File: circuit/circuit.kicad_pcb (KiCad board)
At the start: 2 copper layers, 51.5 x 59 mm, 19 parts, among them J5 PWR1, J6 Signal1, J7 PWR2, J8 Signal2, Q3 BC337, U5 ADuM1250, U6 Optocoupler_DC_PhotoNPN_AKEC, U7 LM7805

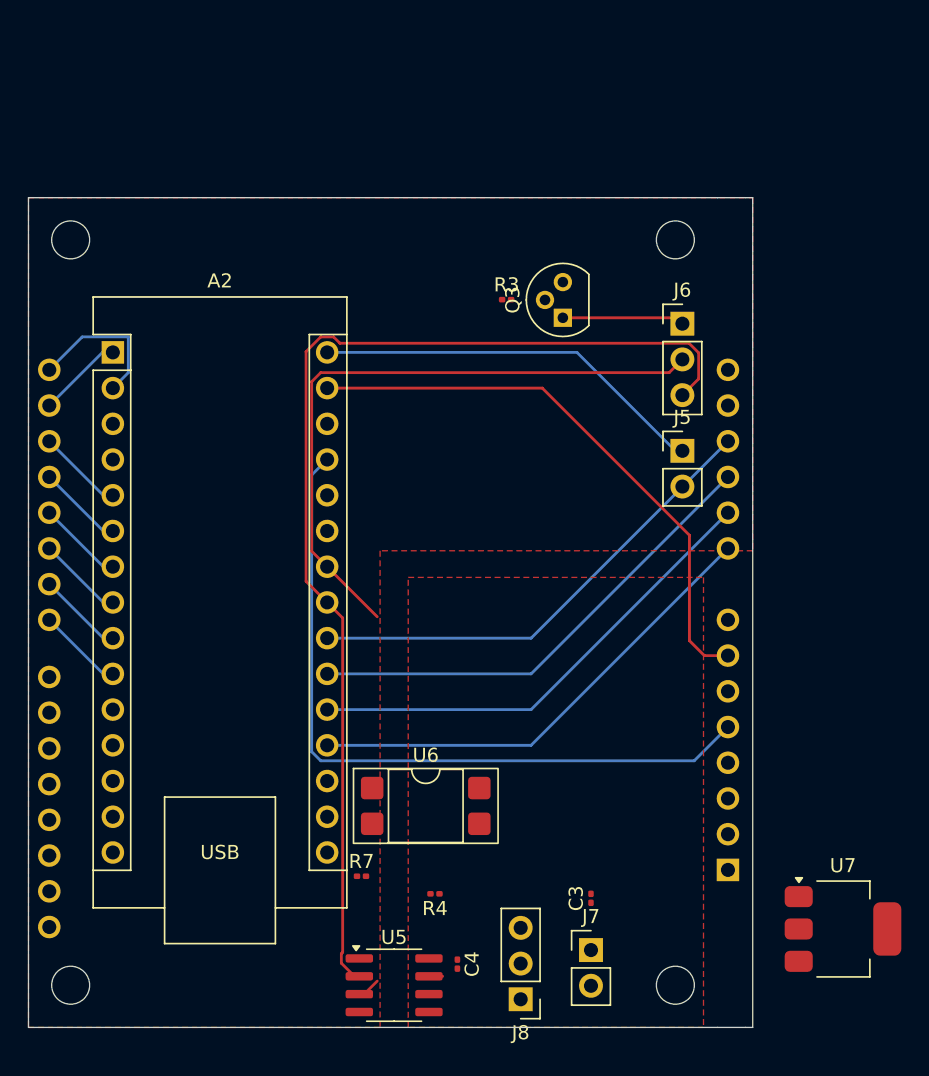
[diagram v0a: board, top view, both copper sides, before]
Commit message: Updated PCB layout and circuit.
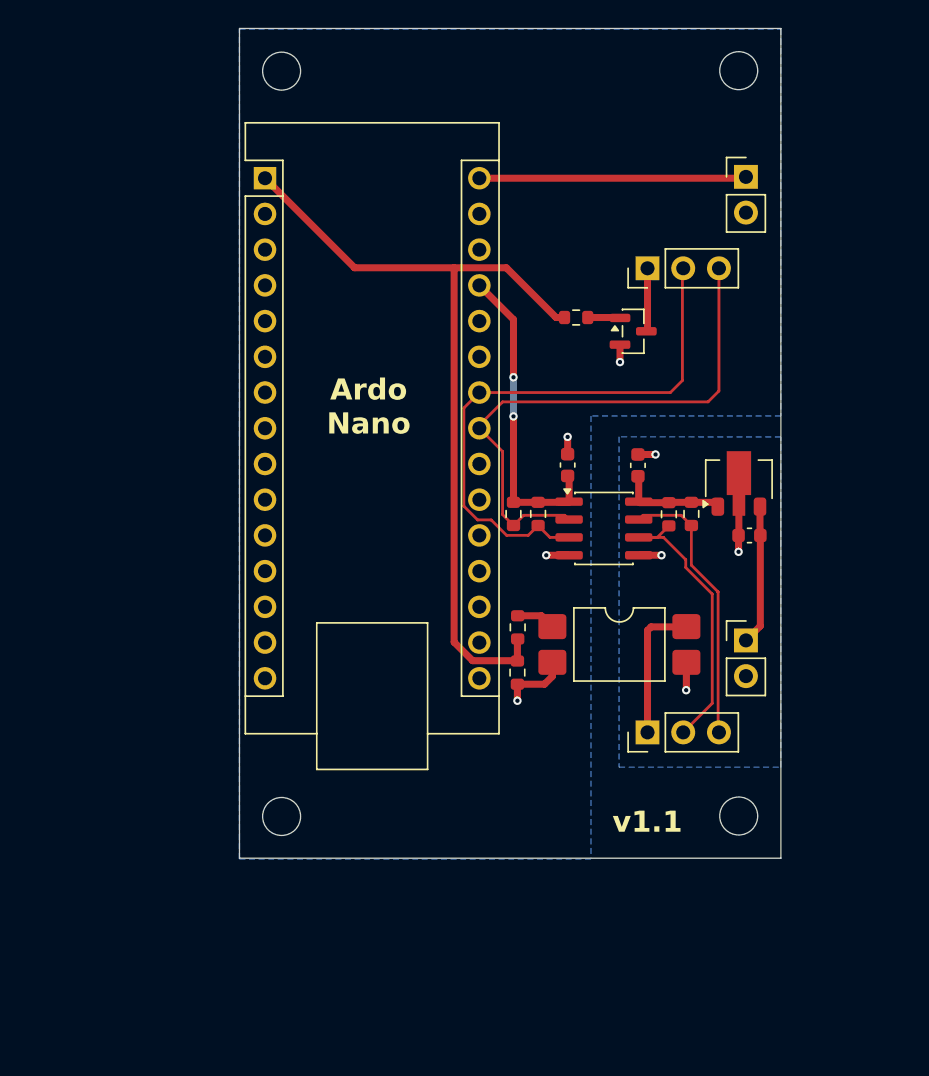
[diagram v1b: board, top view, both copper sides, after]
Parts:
- removed A2: Arduino_Nano_R4, Module:Arduino_Nano
- removed J6: Signal1, Connector_PinHeader_2.54mm:PinHeader_1x03_P2.54mm_Vertical
- removed J7: PWR2, Connector_PinHeader_2.54mm:PinHeader_1x02_P2.54mm_Vertical
- removed J8: Signal2, Connector_PinHeader_2.54mm:PinHeader_1x03_P2.54mm_Vertical
- removed Q3: BC337, Package_TO_SOT_THT:TO-92
- removed the REF** at (67.0, 114.0)
- removed the REF** at (24.0, 114.0)
- removed the REF** at (67.0, 61.0)
- removed the REF** at (24.0, 61.0)
- removed U5: ADuM1250, Package_SO:SOIC-8_3.9x4.9mm_P1.27mm
- removed U6: Optocoupler_DC_PhotoNPN_AKEC, Package_DIP:DIP-4_W7.62mm_SMDSocket_SmallPads
- removed U7: LM7805, Package_TO_SOT_SMD:SOT-223-3_TabPin2
- added C1: 0.1uF, Capacitor_SMD:C_0603_1608Metric, F.Cu at (59.3, 77.0)
- added J2: Conn_01x02_Pin, Connector_PinHeader_2.54mm:PinHeader_1x02_P2.54mm_Vertical, F.Cu at (72.0, 56.5)
- added J3: Conn_01x03_Pin, Connector_PinHeader_2.54mm:PinHeader_1x03_P2.54mm_Vertical, F.Cu at (65.0, 63.0)
- added J4: Conn_01x02_Pin, Connector_PinHeader_2.54mm:PinHeader_1x02_P2.54mm_Vertical, F.Cu at (72.0, 89.5)
- added Q1: BC817, Package_TO_SOT_SMD:SOT-23, F.Cu at (64.0, 67.5)
- added R1: 2,2k, Resistor_SMD:R_0603_1608Metric, F.Cu at (57.2, 80.5)
- added R2: 2,2k, Resistor_SMD:R_0603_1608Metric, F.Cu at (55.5, 80.5)
- added R5: 10k, Resistor_SMD:R_0603_1608Metric, F.Cu at (55.8, 91.8)
- added R6: 4,7k, Resistor_SMD:R_0603_1608Metric, F.Cu at (59.9, 66.5)
- added REF**: MountingHole_2.7mm_M2.5_DIN965, MountingHole:MountingHole_2.7mm_M2.5_DIN965, F.Cu at (39.0, 49.0)
- added REF**: MountingHole_2.7mm_M2.5_DIN965, MountingHole:MountingHole_2.7mm_M2.5_DIN965, F.Cu at (71.5, 102.0)
- added REF**: MountingHole_2.7mm_M2.5_DIN965, MountingHole:MountingHole_2.7mm_M2.5_DIN965, F.Cu at (71.5, 49.0)
- added REF**: MountingHole_2.7mm_M2.5_DIN965, MountingHole:MountingHole_2.7mm_M2.5_DIN965, F.Cu at (39.0, 102.0)
- added U1: L78L05, Package_TO_SOT_SMD:SOT-89-3, F.Cu at (71.5, 78.0)
- added U2: ADuM1250, Package_SO:SOIC-8_3.9x4.9mm_P1.27mm, F.Cu at (61.9, 81.5)
- added U3: LTV-817S, Package_DIP:SMDIP-4_W9.53mm, F.Cu at (63.0, 89.8)
- A1: value TFT Dummy -> Arduino_Nano_R4; footprint Module:Arduino_UNO_R2 -> Module:Arduino_Nano; moved to F.Cu
- C3: value 0.33uF -> 0.1uF; footprint Capacitor_SMD:C_0201_0603Metric -> Capacitor_SMD:C_0603_1608Metric
- C4: value 0.1uF -> 0.33uF; footprint Capacitor_SMD:C_0201_0603Metric -> Capacitor_SMD:C_0603_1608Metric
- J5: value PWR1 -> Conn_01x03_Pin; footprint Connector_PinHeader_2.54mm:PinHeader_1x02_P2.54mm_Vertical -> Connector_PinHeader_2.54mm:PinHeader_1x03_P2.54mm_Vertical
- R3: value 1k -> 2,2k; footprint Resistor_SMD:R_0201_0603Metric -> Resistor_SMD:R_0603_1608Metric
- R4: value 190 -> 2,2k; footprint Resistor_SMD:R_0201_0603Metric -> Resistor_SMD:R_0603_1608Metric
- R7: value 10k -> 1k; footprint Resistor_SMD:R_0201_0603Metric -> Resistor_SMD:R_0603_1608Metric
- moved A1 59.2 mm to (37.8, 56.6), turned to 0 degrees
- moved C4 36.9 mm to (72.3, 82.0), turned to 180 degrees
- moved R4 31.7 mm to (66.5, 80.5), turned to 90 degrees
- moved C3 31.0 mm to (64.3, 77.0)
- moved R7 20.9 mm to (55.8, 88.6), turned to -90 degrees
- moved J5 20.2 mm to (65.0, 96.0), turned to 90 degrees
- moved R3 20.1 mm to (68.1, 80.5), turned to 90 degrees
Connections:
- A1 pad 1: unconnected-(A1-NC-Pad1) -> ENABLE
- A1 pad 10: Net-(A1-A1) -> unconnected-(A1-D7-Pad10)
- A1 pad 11: Net-(A1-A2) -> unconnected-(A1-D8-Pad11)
- A1 pad 12: Net-(A1-A3) -> unconnected-(A1-D9-Pad12)
- A1 pad 15: Net-(A1-D0/RX) -> unconnected-(A1-D12-Pad15)
- A1 pad 16: Net-(A1-D1/TX) -> unconnected-(A1-D13-Pad16)
- A1 pad 17: Net-(A1-D2) -> unconnected-(A1-3V3-Pad17)
- A1 pad 18: Net-(A1-D3) -> unconnected-(A1-AREF-Pad18)
- A1 pad 19: Net-(A1-D4) -> unconnected-(A1-A0-Pad19)
- A1 pad 20: Net-(A1-D5) -> unconnected-(A1-A1-Pad20)
- A1 pad 21: Net-(A1-D6) -> unconnected-(A1-A2-Pad21)
- A1 pad 22: Net-(A1-D7) -> unconnected-(A1-A3-Pad22)
- A1 pad 23: unconnected-(A1-D8-Pad23) -> Net-(A1-A4)
- A1 pad 24: unconnected-(A1-D9-Pad24) -> Net-(A1-A5)
- A1 pad 27: unconnected-(A1-D12-Pad27) -> Net-(A1-+5V)
- A1 pad 29: unconnected-(A1-GND-Pad29) -> GND1
- A1 pad 3: Net-(A1-~{RESET}) -> unconnected-(A1-~{RESET}-Pad3)
- A1 pad 30: unconnected-(A1-AREF-Pad30) -> IN1
- A1 pad 4: unconnected-(A1-3V3-Pad4) -> GND1
- A1 pad 5: Net-(A1-+5V) -> unconnected-(A1-D2-Pad5)
- A1 pad 7: GND1 -> unconnected-(A1-D4-Pad7)
- A1 pad 9: Net-(A1-A0) -> unconnected-(A1-D6-Pad9)
- C3 pad 1: IN2 -> Net-(U1-OUT)
- C4 pad 1: Net-(U5-VDD2) -> IN2
- J5 pad 1: IN1 -> Net-(J5-Pin_1)
- J5 pad 2: GND1 -> Net-(J5-Pin_2)
- R3 pad 1: Net-(Q3-B) -> Net-(J5-Pin_3)
- R3 pad 2: ENABLE -> Net-(U1-OUT)
- R4 pad 1: Net-(R4-Pad1) -> Net-(J5-Pin_2)
- R4 pad 2: ENABLE -> Net-(U1-OUT)
- R7 pad 1: ENABLE -> Net-(R7-Pad1)
- R7 pad 2: GND1 -> ENABLE
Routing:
- net Net-(A2-A4): track 78.6 -> 0.00 mm
- net ENABLE: track 0.00 -> 58.7 mm
- net Net-(A2-A5): track 47.3 -> 0.00 mm
- net Net-(A1-A5): track 0.00 -> 40.3 mm
- net Net-(A1-A4): track 0.00 -> 39.4 mm
- net Net-(A1-A3): track 34.3 -> 0.00 mm
- net Net-(A1-A2): track 34.3 -> 0.00 mm
- net Net-(A1-A1): track 34.3 -> 0.00 mm
- net Net-(A1-A0): track 34.3 -> 0.00 mm
- net GND1: track 40.8 -> 8.97 mm, vias 0 -> 4
- net Net-(A1-+5V): track 52.1 -> 22.3 mm, vias 0 -> 2
- net Net-(J5-Pin_2): track 0.00 -> 20.4 mm
- net Net-(J5-Pin_3): track 0.00 -> 19.7 mm
- net Net-(A1-D0/RX): track 10.7 -> 0.00 mm
- net Net-(J5-Pin_1): track 0.00 -> 10.1 mm
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- added copper zone on B.Cu, net GND1
- added copper zone on B.Cu, net GND2
- removed copper zone on F.Cu, net GND1
- removed copper zone on F.Cu, net GND2
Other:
- board size 51.5 x 59 mm -> 38.5 x 59 mm
- board text added: "Ardo Nano"
- board text added: "v1.1"
